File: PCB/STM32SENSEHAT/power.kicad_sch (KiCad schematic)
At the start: 29 parts, among them IC1 DW01A, Q1 AO3401A, U1 MCP1700x-330xxTT, U2 TP4056, U7 8205A

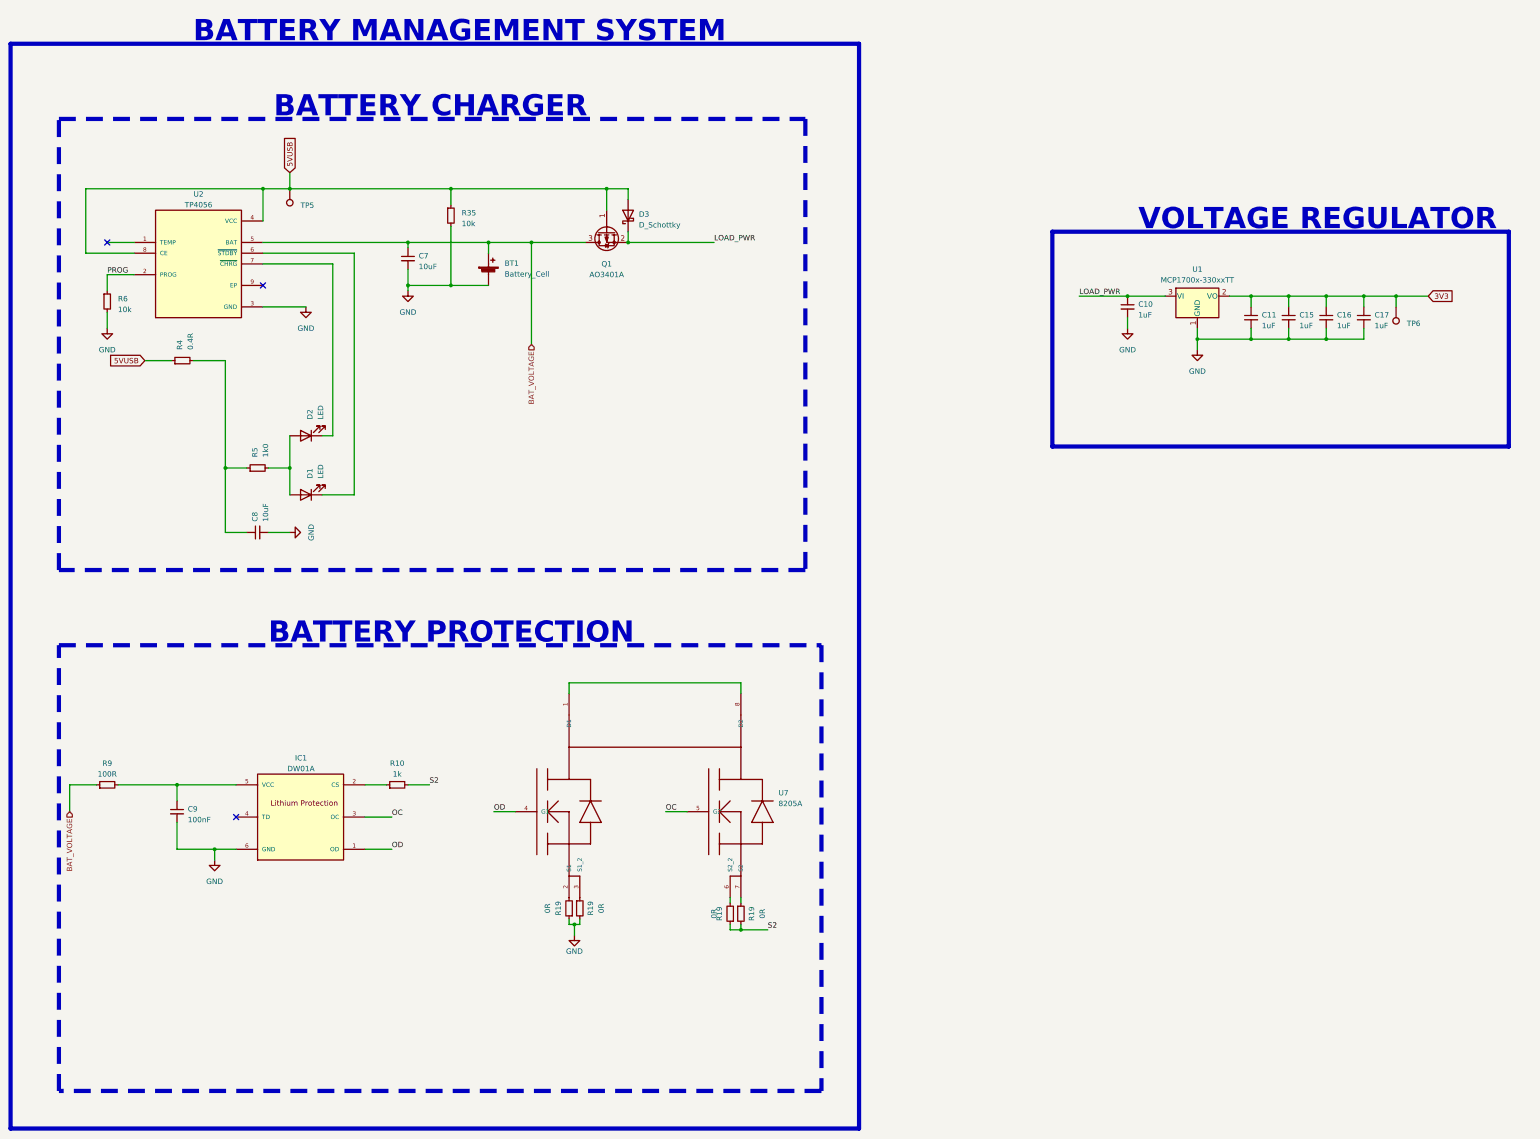
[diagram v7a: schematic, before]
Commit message: Rework of Power,MCU and Sensor Schematic
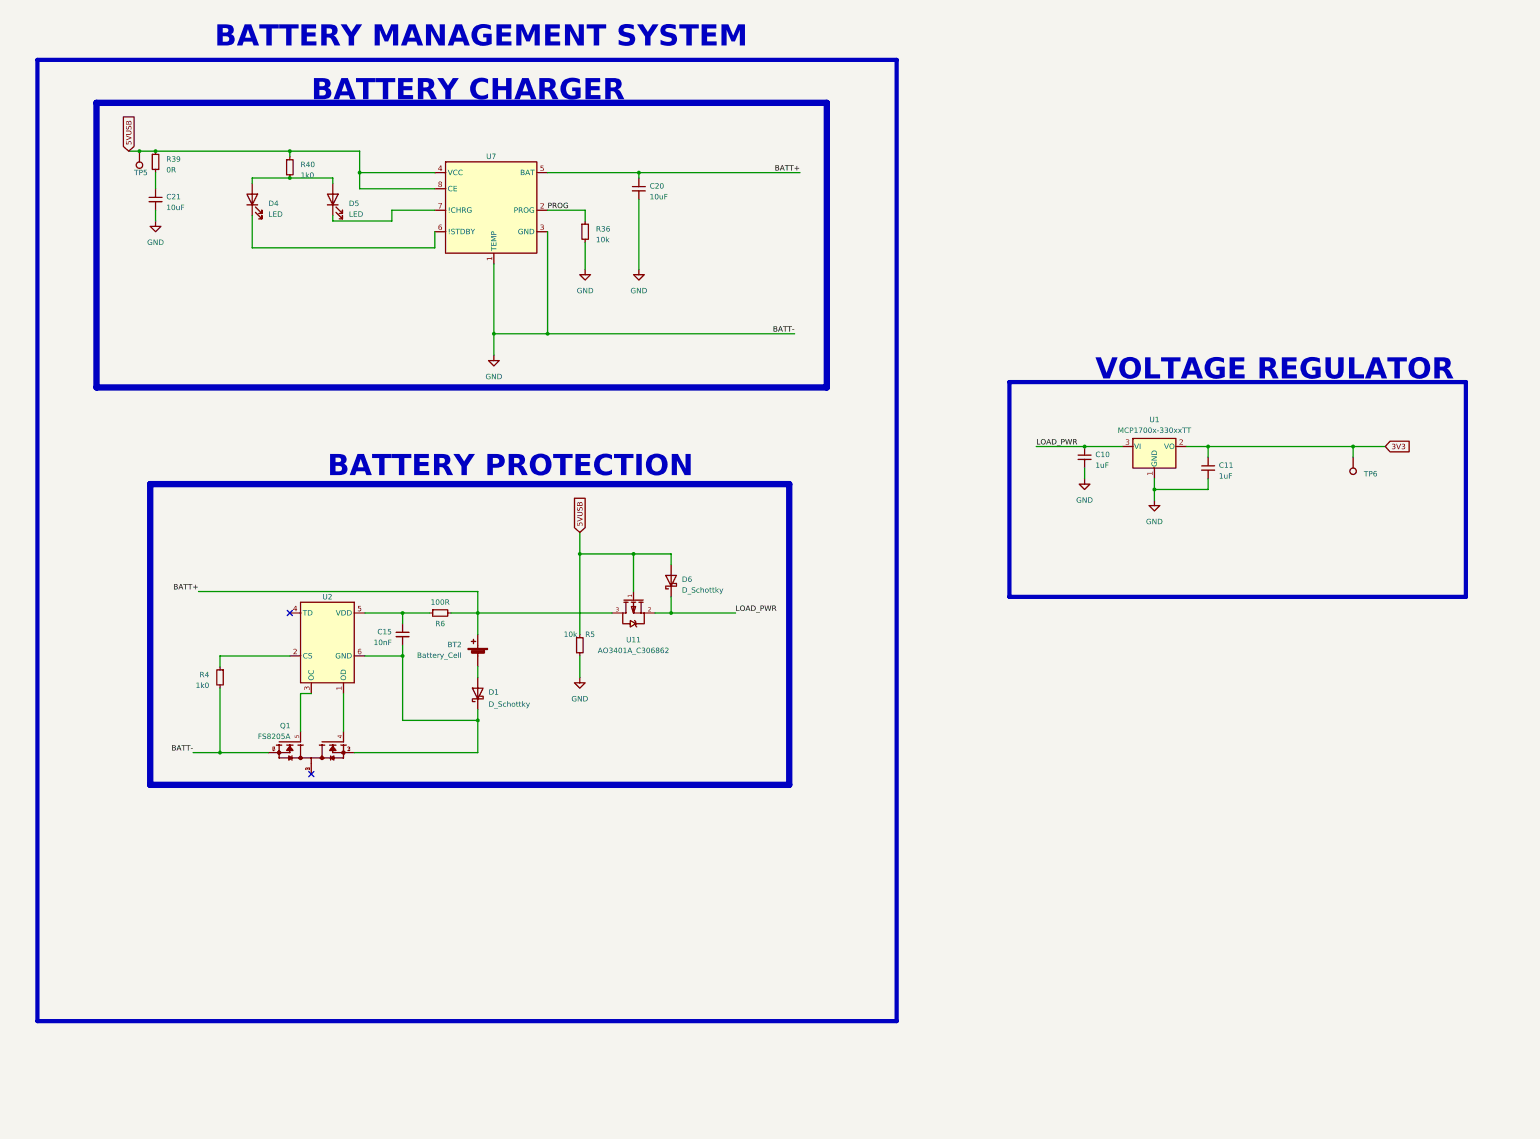
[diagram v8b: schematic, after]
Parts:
- removed BT1: Battery_Cell, Battery:BatteryHolder_Keystone_1042_1x18650, symbol Device:Battery_Cell
- removed C16, C17: 1uF, Capacitor_SMD:C_0805_2012Metric, symbol Device:C_Small
- removed C7, C8: 10uF, Capacitor_SMD:C_0805_2012Metric, symbol Device:C_Small
- removed C9: 100nF, Capacitor_SMD:C_0805_2012Metric, symbol Device:C_Small
- removed D1, D2: LED, LED_THT:LED_D5.0mm, symbol Device:LED
- removed D3: D_Schottky, Package_TO_SOT_SMD:TSOT-23-6, symbol Device:D_Schottky
- removed IC1: DW01A, DW01A:SOT23-6, symbol DW01A:DW01A
- removed Q1: AO3401A, Package_TO_SOT_SMD:SOT-23, symbol Transistor_FET:AO3401A
- removed R10: 1k, Resistor_SMD:R_0603_1608Metric, symbol Device:R_Small
- removed R19 (x4): 0R, Resistor_SMD:R_0805_2012Metric, symbol Device:R_Small
- removed R35: 10k, Resistor_SMD:R_0805_2012Metric, symbol Device:R_Small
- removed R9: 100R, Resistor_SMD:R_0805_2012Metric, symbol Device:R_Small
- removed U2: TP4056, TP4056:SOP127P600X175-9N, symbol TP4056:TP4056
- removed U7: 8205A, 8205A:TSSOP8, symbol 8205A:8205A
- added BT2: Battery_Cell, Battery:BatteryHolder_Keystone_1042_1x18650, symbol Device:Battery_Cell
- added C20, C21: 10uF, JLCfootprint:C0805, symbol Device:C_Small
- added D1, D6: D_Schottky, JLCfootprint:SOT-23-3_L3.0-W1.7-P0.95-LS2.9-BR, symbol Device:D_Schottky
- added D4, D5: LED, LED_THT:LED_D5.0mm, symbol Device:LED
- added Q1: FS8205A, JLCfootprint:TSSOP-8_L4.4-W3.0-P0.65-LS6.4-BL, symbol FS8205A:FS8205A
- added R36: 10k, JLCfootprint:R0805, symbol Device:R_Small
- added R39: 0R, JLCfootprint:R0805, symbol Device:R_Small
- added R40: 1k0, JLCfootprint:R0805, symbol Device:R_Small
- added U11: AO3401A_C306862, JLCfootprint:SOT-23-3_L2.9-W1.3-P1.90-LS2.4-BR, symbol AO3401A_C306862:AO3401A_C306862
- added U2: ~, JLCfootprint:SOT-23-6_L2.9-W1.6-P0.95-LS2.8-BL, symbol UCT:DW01A
- added U7: ~, JLCfootprint:ESOP-8_L4.9-W3.9-P1.27-LS6.0-BL-EP, symbol UCT:TP4056
- C10, C11: footprint Capacitor_SMD:C_0805_2012Metric -> JLCfootprint:C0805
- C15: value 1uF -> 10nF; footprint Capacitor_SMD:C_0805_2012Metric -> JLCfootprint:C0805
- R4: value 0.4R -> 1k0; footprint Resistor_SMD:R_0805_2012Metric -> JLCfootprint:R0805
- R5: value 1k0 -> 10k; footprint Resistor_SMD:R_0603_1608Metric -> JLCfootprint:R0805
- R6: value 10k -> 100R; footprint Resistor_SMD:R_0805_2012Metric -> JLCfootprint:R0805
- U1: footprint Package_TO_SOT_SMD:SOT-23 -> JLCfootprint:SOT-23-3_L2.9-W1.6-P1.90-LS2.8-BR
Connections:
- net 3V3: no longer C15.1
- net 5VUSB: now also R5.1, D6.2 (A), R39.1, R40.1, U11.1 (G), U7.4 (VCC), U7.8 (CE); no longer R4.1
- net GND: now also R4.2, R5.2, C20.2, C21.2, Q1.6, Q1.7, R36.2, U7.1 (TEMP), U7.3 (GND); no longer C15.2, R6.2
- net LOAD_PWR: now also D6.1 (K), U11.2 (S)
- net PROG: now also R36.1, U7.2 (PROG); no longer R6.1
- new net: C15.1, R6.1, U2.5 (VDD)
- new net: C15.2, D1.1 (K), Q1.2, Q1.3, U2.6 (GND)
- new net: D4.2 (A), D5.2 (A), R40.2
- new net: D4.1 (K), U7.6 (!STDBY)
- new net: D5.1 (K), U7.7 (!CHRG)
- new net: Q1.4, U2.1 (OD)
- new net: R4.1, U2.2 (CS)
- new net: Q1.5, U2.3 (OC)
- new net: C21.1, R39.2
- new net: BT2.2 (-), D1.2 (A)
- new net: Q1.1, Q1.8
- new net BATT+: BT2.1 (+), C20.1, R6.2, U11.3 (D), U7.5 (BAT)
- no-connect marks 3 -> 2
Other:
- moved on the sheet: C10, C11, TP6, U1
